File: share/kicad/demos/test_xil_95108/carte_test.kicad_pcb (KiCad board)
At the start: 2 copper layers, 101.6 x 99.7 mm, 42 parts, among them J1 DB25, J2 DB9FEM, K1 CONN_3, P2 CONN_3, P3 CONN_2, P4 CONN_2X2, SW1 SW_PUSH, SW2 SW_PUSH, U1 TDA8702, U2 XC95108PC84, U3 LM7805, U4 74HC04, U5 RAM_32KO, U6 LM318N, X1 10MHz

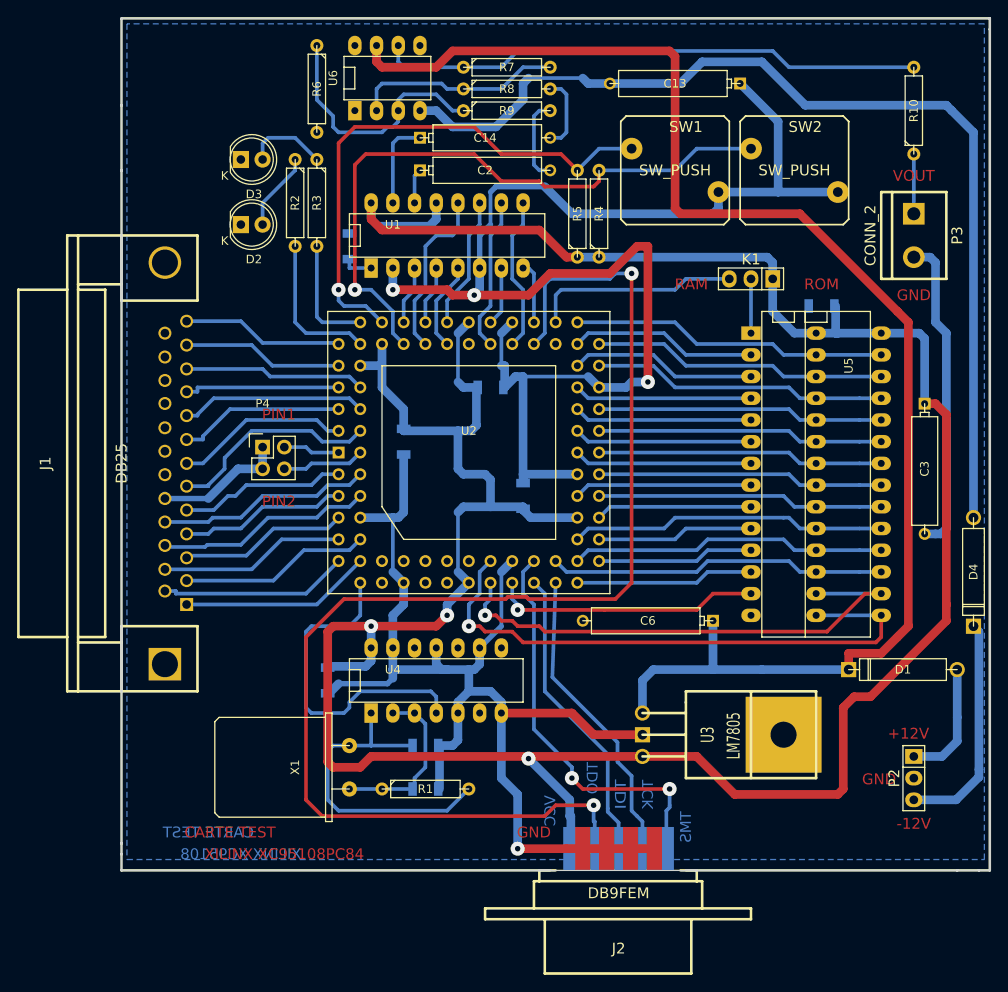
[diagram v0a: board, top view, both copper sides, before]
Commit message: Remove KiCad V4.0.7
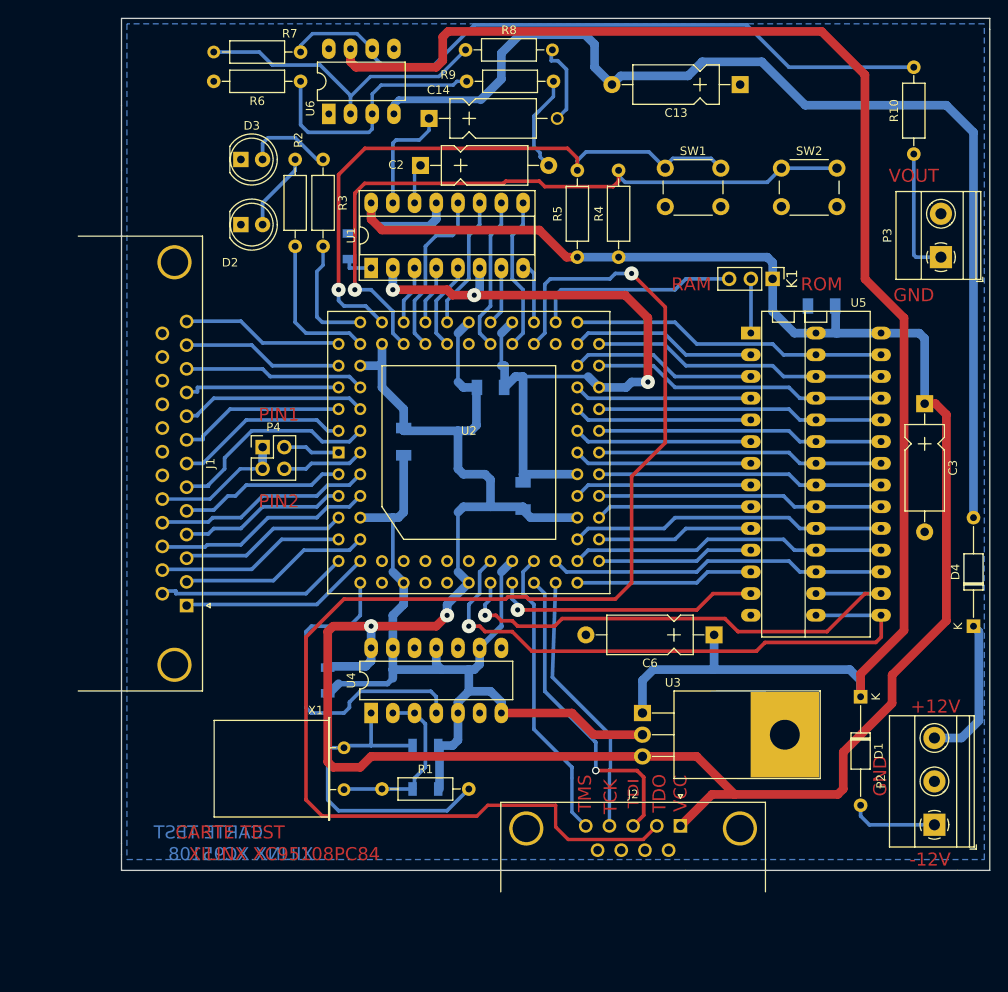
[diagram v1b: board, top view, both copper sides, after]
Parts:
- C10, C11, C7, C8: footprint Capacitors_SMD:C_1206 -> Capacitor_SMD:C_1206_3216Metric_Pad1.24x1.80mm_HandSolder
- C13, C14, C2, C3, C6: footprint Discret:CP6 -> Capacitor_THT:CP_Axial_L10.0mm_D4.5mm_P15.00mm_Horizontal
- D1, D4: footprint Discret:D5 -> Diode_THT:D_DO-35_SOD27_P12.70mm_Horizontal
- D2, D3: footprint LEDs:LED-5MM -> LED_THT:LED_D5.0mm
- J1: footprint Connect:DB25FC -> Connector_Dsub:DSUB-25_Female_Horizontal_P2.77x2.84mm_EdgePinOffset9.90mm_Housed_MountingHolesOffset11.32mm
- J2: footprint Connect:DB9F_CI_INVERT -> Connector_Dsub:DSUB-9_Female_Horizontal_P2.77x2.84mm_EdgePinOffset4.94mm_Housed_MountingHolesOffset7.48mm
- K1: footprint Socket_Strips:Socket_Strip_Straight_1x03 -> Connector_PinHeader_2.54mm:PinHeader_1x03_P2.54mm_Vertical
- P2: footprint Socket_Strips:Socket_Strip_Straight_1x03 -> TerminalBlock_Phoenix:TerminalBlock_Phoenix_MKDS-1,5-3-5.08_1x03_P5.08mm_Horizontal
- P3: footprint Connect:bornier2 -> TerminalBlock_Phoenix:TerminalBlock_Phoenix_MKDS-1,5-2-5.08_1x02_P5.08mm_Horizontal
- P4: footprint Pin_Headers:Pin_Header_Straight_2x02 -> Connector_PinHeader_2.54mm:PinHeader_2x02_P2.54mm_Vertical
- R1, R10, R2, R3, R4, R5, R6, R7, R8, R9: footprint Discret:R4 -> Resistor_THT:R_Axial_DIN0207_L6.3mm_D2.5mm_P10.16mm_Horizontal
- SW1, SW2: footprint Discret:SW_PUSH -> Button_Switch_THT:SW_PUSH_6mm_h4.3mm
- U1: footprint Sockets_DIP:DIP-16__300_ELL -> Package_DIP:DIP-16_W7.62mm_Socket_LongPads
- U3: footprint Discret:LM78XX -> Package_TO_SOT_THT:TO-220-3_Horizontal_TabDown
- U4: footprint Sockets_DIP:DIP-14__300_ELL -> Package_DIP:DIP-14_W7.62mm_LongPads
- U6: footprint Sockets_DIP:DIP-8__300_ELL -> Package_DIP:DIP-8_W7.62mm_LongPads
- X1: footprint Crystals:HC-18UH -> Crystal:Crystal_HC18-U_Horizontal
- moved R7 24.2 mm to (115.6, 40.1), turned to 180 degrees
- moved U5 18.2 mm to (168.3, 73.0), turned to 0 degrees
- moved J1 16.7 mm to (102.2, 104.9), turned to -90 degrees
- moved U1 9.67 mm to (123.8, 65.4), turned to 90 degrees
- moved J2 8.92 mm to (160.0, 130.7), turned to 0 degrees
- moved U4 8.52 mm to (123.8, 117.5), turned to 90 degrees
- moved U6 8.04 mm to (118.9, 47.4), turned to 90 degrees
- moved C6 7.92 mm to (164.0, 108.3)
- moved C13 7.62 mm to (167.0, 43.9)
- moved C3 7.62 mm to (188.6, 81.3)
- moved C2 7.58 mm to (129.6, 53.4)
- moved C14 6.94 mm to (130.6, 47.9)
- moved R8 6.65 mm to (134.9, 39.9)
- moved D4 6.35 mm to (194.3, 107.3), turned to 90 degrees
- moved P2 5.97 mm to (189.7, 130.6)
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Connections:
- net /PAR_AUX0/STROBE* renamed /PAR_AUX0/STROBE*
- net /PAR_AUX1/ERROR* renamed /PAR_AUX1/ERROR*
- net /PAR_AUX2/AUTOLF* renamed /PAR_AUX2/AUTOLF*
- net /PAR_AUX3/SELECT* renamed /PAR_AUX3/SELECT*
- net /PAR_AUX4/PE renamed /PAR_AUX4/PE
- net /PAR_AUX5/BUSY* renamed /PAR_AUX5/BUSY*
- net /PAR_AUX6/ACK renamed /PAR_AUX6/ACK
- net /PAR_AUX7/INIT renamed /PAR_AUX7/INIT
- net /PAR_AUX8/SELECT renamed /PAR_AUX8/SELECT
- net /R/W-A14 renamed /R/W-A14
- net /XIN/CLK renamed /XIN/CLK
- U2 pad 14: Net-(U2-Pad14) -> unconnected-(U2-Pad14)
- U2 pad 15: Net-(U2-Pad15) -> unconnected-(U2-Pad15)
- U2 pad 17: Net-(U2-Pad17) -> unconnected-(U2-Pad17)
- U2 pad 18: Net-(U2-Pad18) -> unconnected-(U2-Pad18)
- U2 pad 19: Net-(U2-Pad19) -> unconnected-(U2-Pad19)
- U2 pad 20: Net-(U2-Pad20) -> unconnected-(U2-Pad20)
- U2 pad 21: Net-(U2-Pad21) -> unconnected-(U2-Pad21)
- U2 pad 23: Net-(U2-Pad23) -> unconnected-(U2-Pad23)
- U2 pad 57: Net-(U2-Pad57) -> unconnected-(U2-Pad57)
- U2 pad 65: Net-(U2-Pad65) -> unconnected-(U2-Pad65)
- U4 pad 10: Net-(U4-Pad10) -> unconnected-(U4-Pad10)
- U4 pad 12: Net-(U4-Pad12) -> unconnected-(U4-Pad12)
- U4 pad 6: Net-(U4-Pad6) -> unconnected-(U4-Pad6)
- U4 pad 8: Net-(U4-Pad8) -> unconnected-(U4-Pad8)
- U6 pad 1: Net-(U6-Pad1) -> unconnected-(U6-Pad1)
- U6 pad 5: Net-(U6-Pad5) -> unconnected-(U6-Pad5)
- U6 pad 8: Net-(U6-Pad8) -> unconnected-(U6-Pad8)
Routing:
- net GND: track 361.0 -> 212.2 mm, vias 4 -> 3
- net Net-(R10-Pad2): track 64.1 -> 79.3 mm
- net /TMS: track 47.4 -> 34.6 mm, vias 2 -> 0
- net +12V: track 168.7 -> 180.6 mm
- net Net-(R7-Pad2): track 24.4 -> 36.0 mm
- net /SW0: track 62.8 -> 72.2 mm
- net /-12BATT: track 26.6 -> 17.4 mm
- net /TDO: track 154.6 -> 163.8 mm, vias 2 -> 1
- net -12V: track 118.9 -> 127.7 mm
- net Net-(P3-Pad1): track 6.98 -> 15.1 mm
- net VCC: track 345.6 -> 338.4 mm, vias 3 -> 2
- net /SW1: track 75.5 -> 81.6 mm
- net /TCK: track 35.5 -> 31.3 mm
- net /+12BATT: track 14.2 -> 10.3 mm
- net Net-(C14-Pad1): track 10.4 -> 13.2 mm
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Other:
- net class Default removed
- rule pad_to_mask_clearance: 0.254 -> 0
